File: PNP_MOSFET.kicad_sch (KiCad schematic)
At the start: 8 parts, among them Q3 BSS138, Q4 BSS84

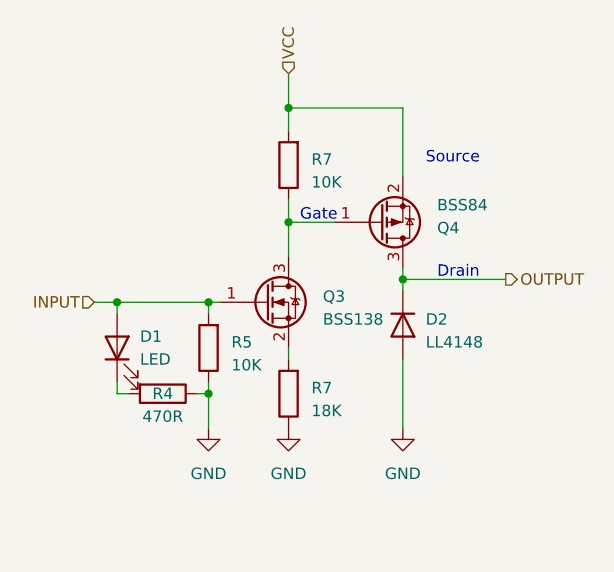
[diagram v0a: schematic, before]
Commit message: Fixed some design flaws, first version didn't work.
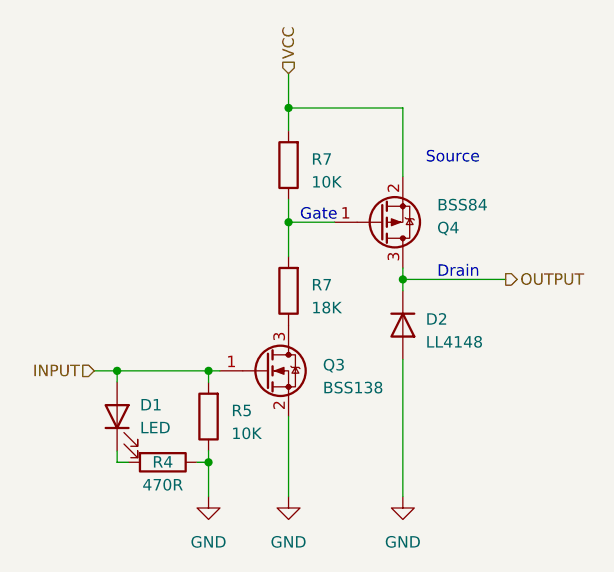
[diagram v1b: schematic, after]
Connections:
- net GND: now also Q3.2 (S); no longer R7.1
- net at R7.2: now also Q4.1 (G), R7.1; no longer Q3.2 (S)
- new net: Q3.3 (D), R7.1
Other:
- moved on the sheet: D1, Q3, R4, R5, R7
